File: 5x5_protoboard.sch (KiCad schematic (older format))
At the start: 82 parts, among them CON1 BARREL_JACK, CON2 USB-MINI-B, CON3 USB-MICRO, J1 PINS_3X1, J10 PINS_3X1, J11 PINS_3X1, J12 PINS_3X1, J13 PINS_3X1, J14 PINS_3X1, J15 PINS_3X1, J16 PINS_3X1, J17 PINS_3X1, J18 PINS_3X1, J19 PINS_3X1, J2 PINS_3X1, J20 PINS_3X1, J21 PINS_3X1, J22 PINS_3X1, J23 PINS_3X1, J24 PINS_3X1, J25 PINS_3X1, J26 PINS_3X1, J27 PINS_3X1, J28 PINS_3X1, J29 PINS_3X1, J3 PINS_3X1, J30 PINS_3X1, J31 PINS_3X1, J32 PINS_3X1, J33 PINS_3X1, J34 PINS_3X1, J35 PINS_3X1, J36 PINS_3X1, J37 PINS_3X1, J38 PINS_3X1, J39 PINS_3X1, J4 PINS_3X1, J40 PINS_3X1, J41 PINS_3X1, J42 PINS_3X1, J43 PINS_3X1, J44 PINS_3X1, J45 PINS_3X1, J46 PINS_3X1, J47 PINS_3X1, J48 PINS_3X1, J49 PINS_3X1, J5 PINS_3X1, J50 PINS_3X1, J51 PINS_3X1, J52 PINS_3X1, J53 PINS_3X1, J54 PINS_3X1, J55 PINS_3X1, J56 PINS_3X1, J57 PINS_3X1, J58 PINS_3X1, J59 PINS_3X1, J6 PINS_3X1, J60 PINS_3X1, J61 PINS_3X1, J62 PINS_3X1, J63 PINS_3X1, J64 PINS_3X1, J65 PINS_2X1, J7 PINS_3X1, J8 PINS_3X1, J9 PINS_3X1, P1 CONN_5, U1 7805

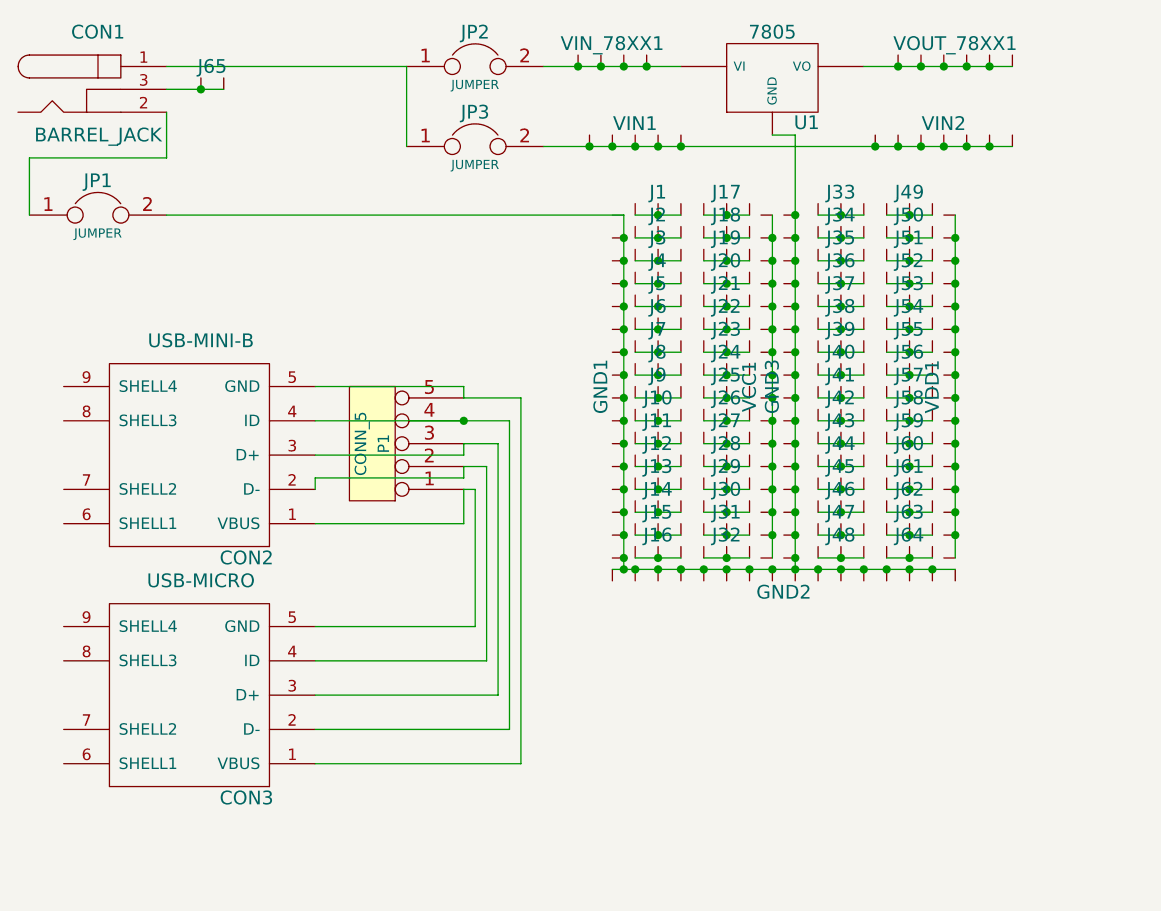
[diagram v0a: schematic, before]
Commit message: added pads for PTC 1812(SMD) fuse on both sides of the PCB between GND and the barrel jack on the same spot as the jumper and in parallel with it and eachother
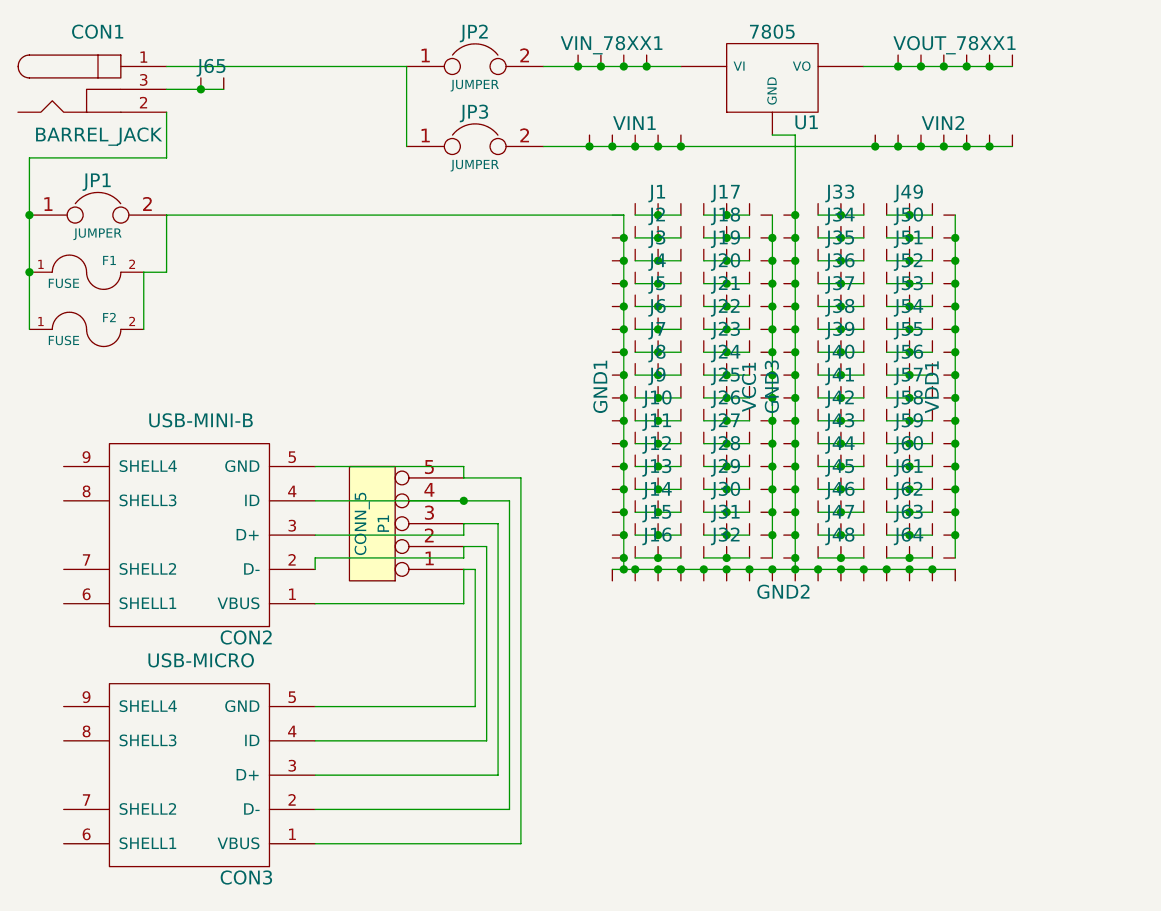
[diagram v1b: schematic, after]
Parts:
- added F1, F2: FUSE, ~, symbol FUSE
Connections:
- net at GND1.1, GND1.10, GND1.11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: now also F1.2, F2.2
- net at CON1.2, JP1.1: now also F1.1, F2.1
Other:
- moved on the sheet: CON2, CON3, P1
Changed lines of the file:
@@
 LIBS:contrib
 LIBS:valves
+LIBS:5x5_protoboard-cache
 LIBS:dp_devices
 LIBS:5x5_protoboard-cache
@@
 L CONN_5 P1
 U 1 1 53DD87F2
-P 4050 4100
-F 0 "P1" V 4000 4100 50  0000 C CNN
-F 1 "CONN_5" V 4100 4100 50  0000 C CNN
-F 2 "~" H 4050 4100 60  0000 C CNN
-F 3 "~" H 4050 4100 60  0000 C CNN
-	1    4050 4100
+P 4050 4450
+F 0 "P1" V 4000 4450 50  0000 C CNN
+F 1 "CONN_5" V 4100 4450 50  0000 C CNN
+F 2 "~" H 4050 4450 60  0000 C CNN
+F 3 "~" H 4050 4450 60  0000 C CNN
+	1    4050 4450
 	-1   0    0    1
 $EndComp
@@
 L USB-MINI-B CON2
 U 1 1 53DD8801
-P 3250 4150
-F 0 "CON2" H 3000 4600 60  0000 C CNN
-F 1 "USB-MINI-B" H 3200 3650 60  0000 C CNN
-F 2 "~" H 3250 4150 60  0000 C CNN
-F 3 "~" H 3250 4150 60  0000 C CNN
-	1    3250 4150
+P 3250 4500
+F 0 "CON2" H 3000 4950 60  0000 C CNN
+F 1 "USB-MINI-B" H 3200 4000 60  0000 C CNN
+F 2 "~" H 3250 4500 60  0000 C CNN
+F 3 "~" H 3250 4500 60  0000 C CNN
+	1    3250 4500
 	-1   0    0    1
 $EndComp
@@
 L USB-MINI-B CON3
 U 1 1 53DD8824
-P 3250 5200
-F 0 "CON3" H 3000 5650 60  0000 C CNN
-F 1 "USB-MICRO" H 3200 4700 60  0000 C CNN
-F 2 "~" H 3250 5200 60  0000 C CNN
-F 3 "~" H 3250 5200 60  0000 C CNN
-	1    3250 5200
+P 3250 5550
+F 0 "CON3" H 3000 6000 60  0000 C CNN
+F 1 "USB-MICRO" H 3200 5050 60  0000 C CNN
+F 2 "~" H 3250 5550 60  0000 C CNN
+F 3 "~" H 3250 5550 60  0000 C CNN
+	1    3250 5550
 	-1   0    0    1
 $EndComp
@@
 	3150 2850 2550 2850
 Wire Wire Line
-	2550 2850 2550 3100
+	2550 2850 2550 3600
 Wire Wire Line
 	3150 3100 5150 3100
@@
 Connection ~ 5900 3100
 Wire Wire Line
-	3800 4450 4450 4450
-Wire Wire Line
-	4450 4450 4450 4300
-Wire Wire Line
-	3800 4300 3800 4250
-Wire Wire Line
-	3800 4250 4450 4250
-Wire Wire Line
-	4450 4250 4450 4200
-Wire Wire Line
-	3800 4150 4450 4150
-Wire Wire Line
-	4450 4150 4450 4100
-Wire Wire Line
-	3800 4000 4650 4000
-Wire Wire Line
-	3800 3850 4450 3850
-Wire Wire Line
-	4450 3850 4450 3900
-Wire Wire Line
-	3800 4900 4500 4900
-Wire Wire Line
-	4500 4900 4500 4300
-Wire Wire Line
-	4500 4300 4450 4300
-Wire Wire Line
-	3800 5050 4550 5050
-Wire Wire Line
-	4550 5050 4550 4200
-Wire Wire Line
-	4550 4200 4450 4200
-Wire Wire Line
-	3800 5200 4600 5200
-Wire Wire Line
-	4600 5200 4600 4100
-Wire Wire Line
-	4600 4100 4450 4100
-Wire Wire Line
-	3800 5350 4650 5350
-Wire Wire Line
-	4650 5350 4650 4000
-Wire Wire Line
-	3800 5500 4700 5500
-Wire Wire Line
-	4700 5500 4700 3900
-Wire Wire Line
-	4700 3900 4450 3900
-Connection ~ 4450 4000
+	3800 4800 4450 4800
+Wire Wire Line
+	4450 4800 4450 4650
+Wire Wire Line
+	3800 4650 3800 4600
+Wire Wire Line
+	3800 4600 4450 4600
+Wire Wire Line
+	4450 4600 4450 4550
+Wire Wire Line
+	3800 4500 4450 4500
+Wire Wire Line
+	4450 4500 4450 4450
+Wire Wire Line
+	3800 4350 4650 4350
+Wire Wire Line
+	3800 4200 4450 4200
+Wire Wire Line
+	4450 4200 4450 4250
+Wire Wire Line
+	3800 5250 4500 5250
+Wire Wire Line
+	4500 5250 4500 4650
+Wire Wire Line
+	4500 4650 4450 4650
+Wire Wire Line
+	3800 5400 4550 5400
+Wire Wire Line
+	4550 5400 4550 4550
+Wire Wire Line
+	4550 4550 4450 4550
+Wire Wire Line
+	3800 5550 4600 5550
+Wire Wire Line
+	4600 5550 4600 4450
+Wire Wire Line
+	4600 4450 4450 4450
+Wire Wire Line
+	3800 5700 4650 5700
+Wire Wire Line
+	4650 5700 4650 4350
+Wire Wire Line
+	3800 5850 4700 5850
+Wire Wire Line
+	4700 5850 4700 4250
+Wire Wire Line
+	4700 4250 4450 4250
+Connection ~ 4450 4350
+$Comp
+L FUSE F1
+U 1 1 53DDB6F8
+P 2800 3350
+F 0 "F1" H 2900 3400 40  0000 C CNN
+F 1 "FUSE" H 2700 3300 40  0000 C CNN
+F 2 "~" H 2800 3350 60  0000 C CNN
+F 3 "~" H 2800 3350 60  0000 C CNN
+	1    2800 3350
+	1    0    0    -1
+$EndComp
+$Comp
+L FUSE F2
+U 1 1 53DDB707
+P 2800 3600
+F 0 "F2" H 2900 3650 40  0000 C CNN
+F 1 "FUSE" H 2700 3550 40  0000 C CNN
+F 2 "~" H 2800 3600 60  0000 C CNN
+F 3 "~" H 2800 3600 60  0000 C CNN
+	1    2800 3600
+	1    0    0    -1
+$EndComp
+Connection ~ 2550 3100
+Connection ~ 2550 3350
+Wire Wire Line
+	3050 3600 3050 3350
+Wire Wire Line
+	3050 3350 3150 3350
+Wire Wire Line
+	3150 3350 3150 3100
 $EndSCHEMATC

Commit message: recreated board using interconnect modules increased rails/triplet pad size, added solder jumper in addition to pin jumpers and added text for USB micro/mini pinout
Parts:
- added JP4, JP5, JP6: JUMPER, ~, symbol JUMPER
- VIN1: value PINS_5X1 -> PINS_4X1; symbol PINS_5X1 -> PINS_4X1
- VIN2: value PINS_7X1 -> PINS_6X1; symbol PINS_7X1 -> PINS_6X1
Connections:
- net at VDD1.1, VDD1.10, VDD1.11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: now also JP5.1
- net at VCC1.1, VCC1.10, VCC1.11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: now also JP4.1
- net at U1.VO, VOUT_78XX1.1, VOUT_78XX1.2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: now also JP6.2
- net at JP3.2, VIN1.1, VIN1.2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: now also JP4.2, JP5.2, JP6.1; no longer VIN1.5, VIN2.7
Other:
- moved on the sheet: GND1, GND2, GND3, J1, J10, J11, J12, J13, J14, J15, J16, J17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

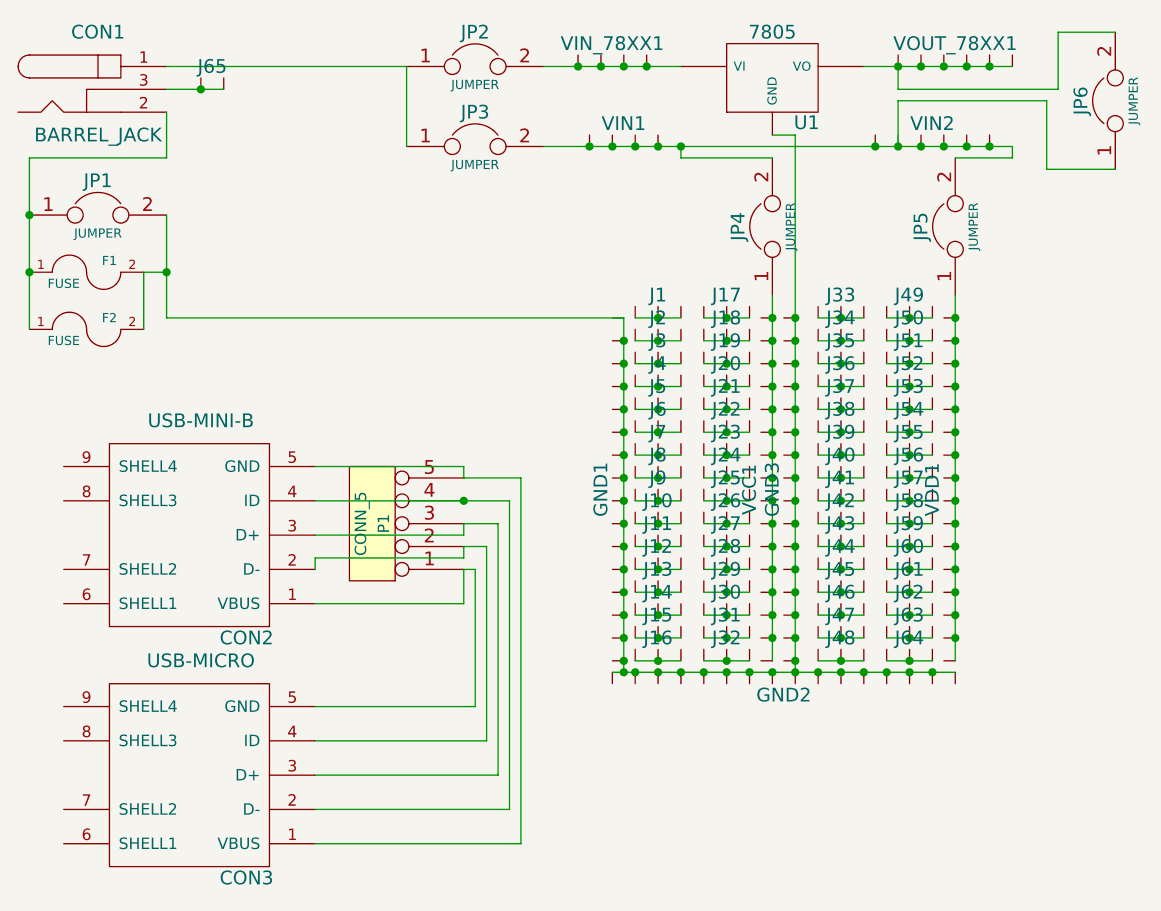
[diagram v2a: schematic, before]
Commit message: added 0603 suppersion caps to 78xx regulator
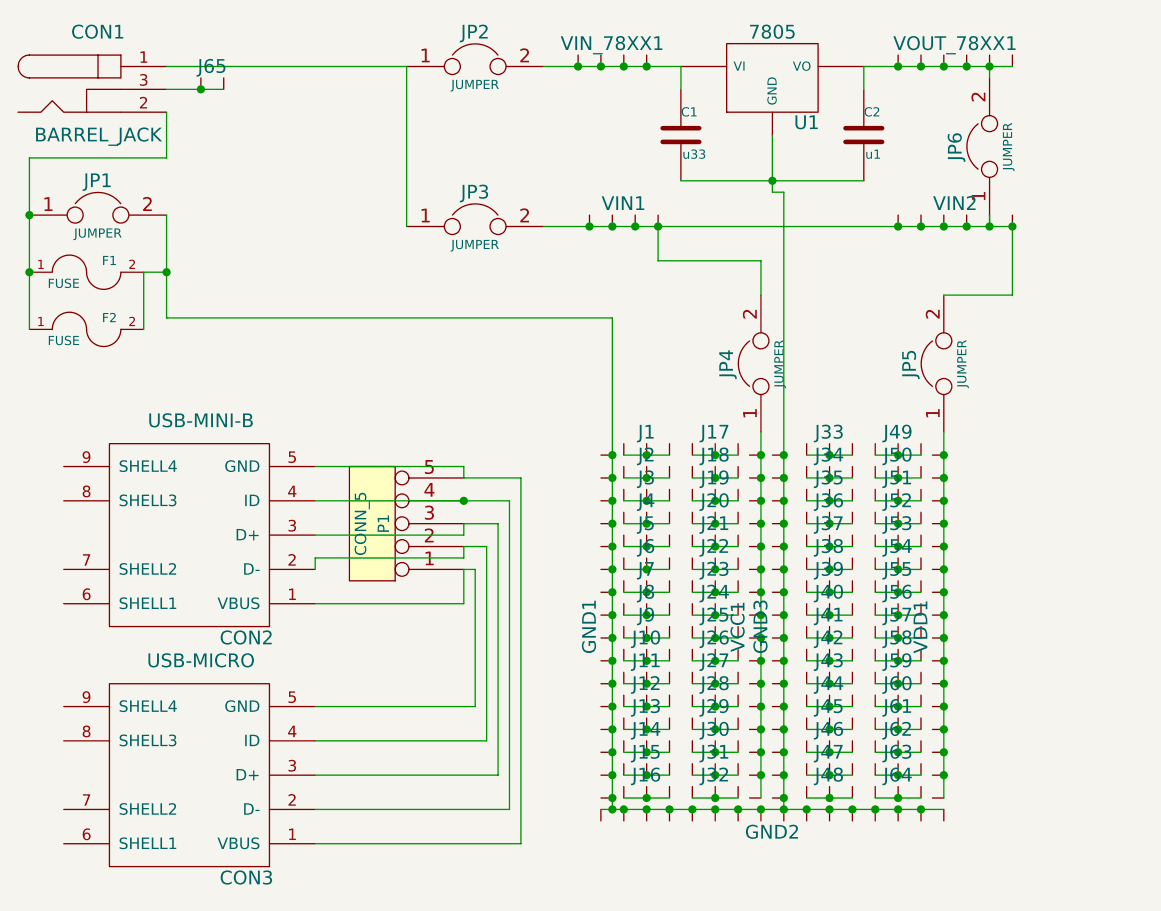
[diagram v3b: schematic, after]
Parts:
- added C1: u33, ~, symbol C
- added C2: u1, ~, symbol C
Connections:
- net at F1.2, F2.2, GND1.1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: now also C1.2, C2.2
- net at JP2.2, U1.VI, VIN_78XX1.1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: now also C1.1
- net at JP6.2, U1.VO, VOUT_78XX1.1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: now also C2.1
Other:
- moved on the sheet: GND1, GND2, GND3, J1, J10, J11, J12, J13, J14, J15, J16, J17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

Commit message: changed interconnect to only have exposed copper on the bottom side, and shorted the jumper on the front side
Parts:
- GND1, GND2, GND3, VCC1, VDD1: value PINS_16X1 -> INTERCONNECT_16X1; symbol PINS_16X1 -> INTERCONNECT_16X1
- J1, J10, J11, J12, J13, J14, J15, J16, J17, J18, J19, J2, J20, J21, J22, J23, J24, J25, J26, J27, J28, J29, J3, J30, J31, J32, J33, J34, J35, J36, J37, J38, J39, J4, J40, J41, J42, J43, J44, J45, J46, J47, J48, J49, J5, J50, J51, J52, J53, J54, J55, J56, J57, J58, J59, J6, J60, J61, J62, J63, J64, J7, J8, J9: value PINS_3X1 -> INTERCONNECT_3X1; symbol PINS_3X1 -> INTERCONNECT_3X1
- J65: value PINS_2X1 -> INTERCONNECT_2X1; symbol PINS_2X1 -> INTERCONNECT_2X1
- VIN1, VIN_78XX1: value PINS_4X1 -> INTERCONNECT_4X1; symbol PINS_4X1 -> INTERCONNECT_4X1
- VIN2, VOUT_78XX1: value PINS_6X1 -> INTERCONNECT_6X1; symbol PINS_6X1 -> INTERCONNECT_6X1
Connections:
- net at C1.1, JP2.2, U1.VI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: no longer VIN_78XX1.2, VIN_78XX1.3, VIN_78XX1.4
- net at CON1.3, J65.1: no longer J65.2
- new net: C1.2, C2.2, F1.2, F2.2, GND1.1, GND2.1, GND3.1, JP1.2, U1.GND
- new net: JP5.1, VDD1.1
- new net: JP4.1, VCC1.1
- new net: C2.1, JP6.2, U1.VO, VOUT_78XX1.1
- new net: JP3.2, JP4.2, JP5.2, JP6.1, VIN1.1, VIN2.1
- now unconnected: J1.1, J10.1, J11.1, J12.1, J13.1, J14.1, J15.1, J16.1, J17.1, J18.1, J19.1, J2.1, J20.1, J21.1, J22.1, J23.1, J24.1, J25.1, J26.1, J27.1, J28.1, J29.1, J3.1, J30.1, J31.1, J32.1, J33.1, J34.1, J35.1, J36.1, J37.1, J38.1, J39.1, J4.1, J40.1, J41.1, J42.1, J43.1, J44.1, J45.1, J46.1, J47.1, J48.1, J49.1, J5.1, J50.1, J51.1, J52.1, J53.1, J54.1, J55.1, J56.1, J57.1, J58.1, J59.1, J6.1, J60.1, J61.1, J62.1, J63.1, J64.1, J7.1, J8.1, J9.1
